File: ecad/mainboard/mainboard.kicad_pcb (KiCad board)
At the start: 12 copper layers, 26 parts, among them M1 Left Motor, M2 Right Motor, Q1 SS8050, Q2 SS8050, U1 LM358

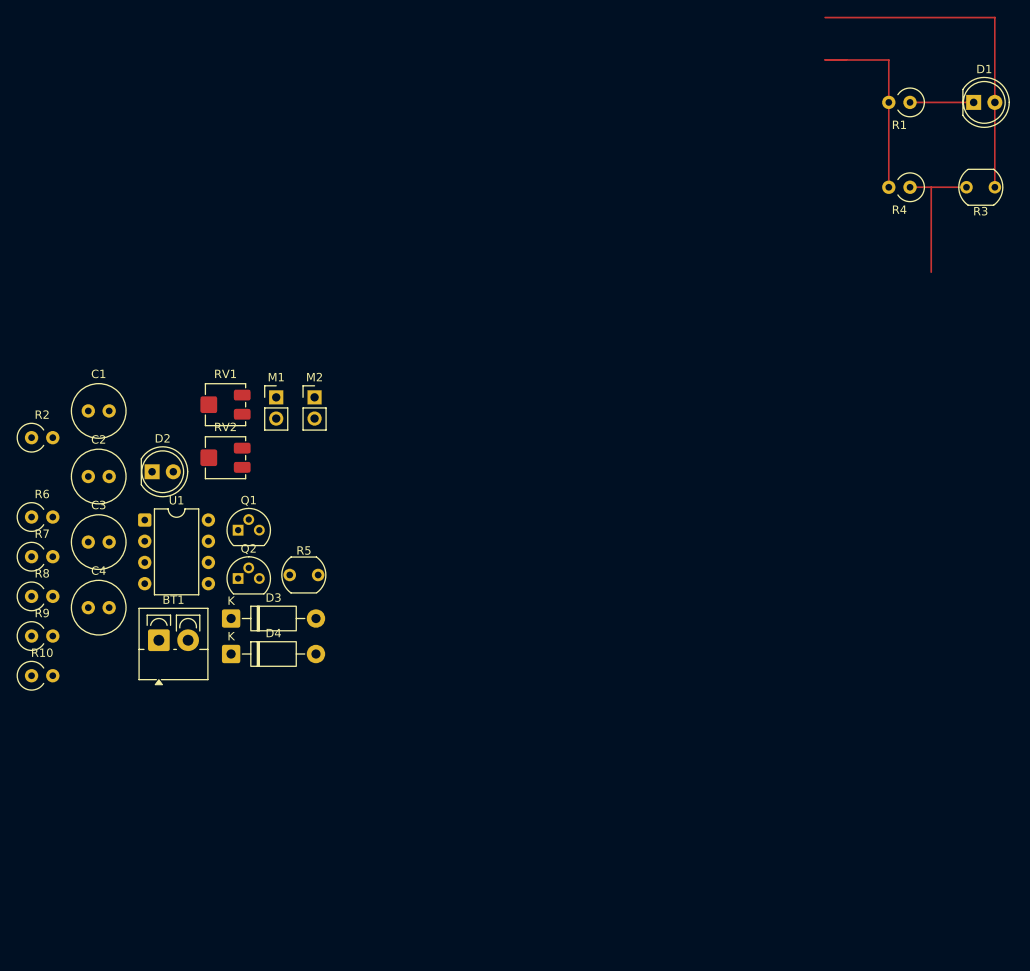
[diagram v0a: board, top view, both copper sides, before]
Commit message: update schematics with smd components
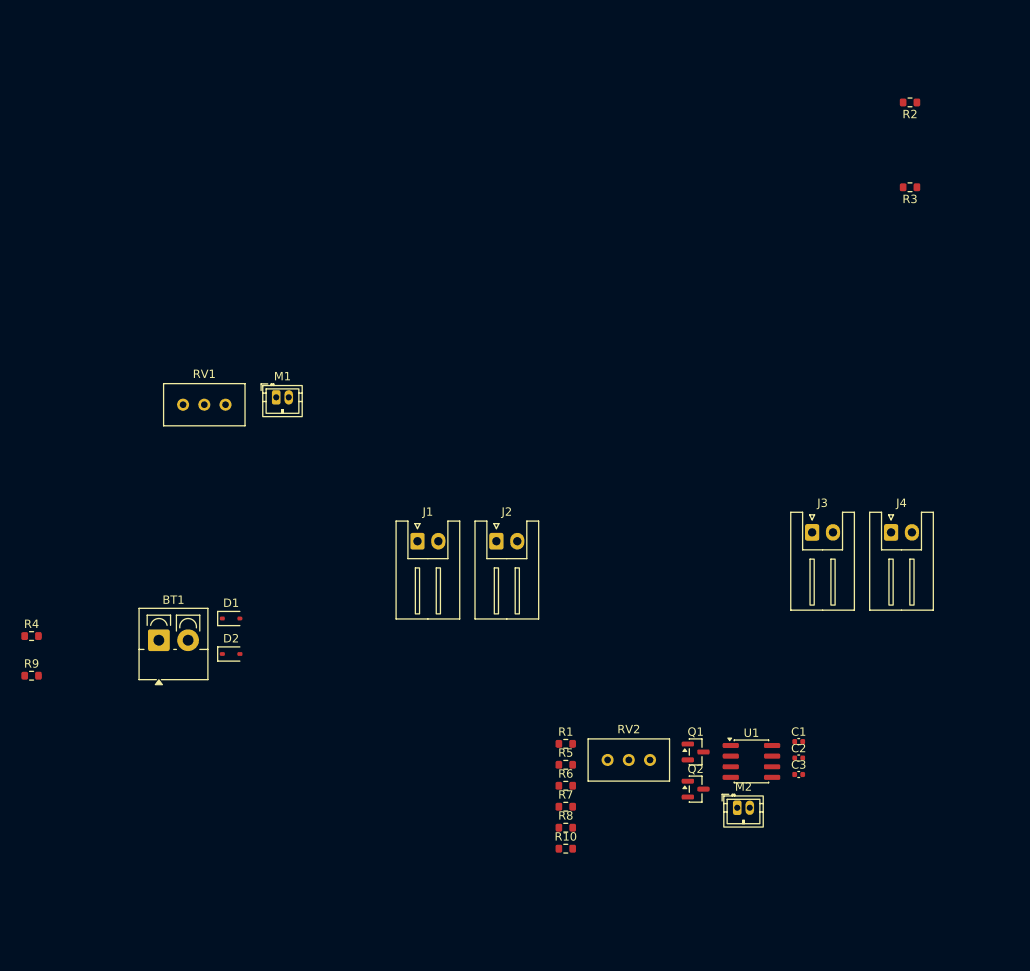
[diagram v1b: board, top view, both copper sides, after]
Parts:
- removed C4: 100uF, Capacitor_THT:C_Radial_D6.3mm_H11.0mm_P2.50mm
- removed the D1 at (180.3, 33.0)
- removed the D2 at (82.0, 77.2)
- removed the R2 at (67.5, 73.2)
- removed the R3 at (182.9, 43.2)
- added J1: IR LED, Connector_JST:JST_XH_S2B-XH-A_1x02_P2.50mm_Horizontal, F.Cu at (113.8, 85.6)
- added J2: IR Diode, Connector_JST:JST_XH_S2B-XH-A_1x02_P2.50mm_Horizontal, F.Cu at (123.2, 85.6)
- added J3: IR LED, Connector_JST:JST_XH_S2B-XH-A_1x02_P2.50mm_Horizontal, F.Cu at (161.0, 84.5)
- added J4: IR Diode, Connector_JST:JST_XH_S2B-XH-A_1x02_P2.50mm_Horizontal, F.Cu at (170.4, 84.5)
- added R1: 2.2k, Resistor_SMD:R_0603_1608Metric, F.Cu at (131.5, 109.8)
- added R10: 10k, Resistor_SMD:R_0603_1608Metric, F.Cu at (131.5, 122.4)
- C1, C2, C3: footprint Capacitor_THT:C_Radial_D6.3mm_H5.0mm_P2.50mm -> Capacitor_SMD:C_0402_1005Metric
- D1: renamed from D3; value 1N4007 -> 1N4148WS; footprint Diode_THT:D_DO-41_SOD81_P10.16mm_Horizontal -> Diode_SMD:D_SOD-323
- D2: renamed from D4; value 1N4007 -> 1N4148WS; footprint Diode_THT:D_DO-41_SOD81_P10.16mm_Horizontal -> Diode_SMD:D_SOD-323
- M1: value Left Motor -> Left N20 Motor; footprint Connector_PinHeader_2.54mm:PinHeader_1x02_P2.54mm_Vertical -> Connector_JST:JST_ZH_B2B-ZR_1x02_P1.50mm_Vertical
- M2: value Right Motor -> Right N20 Motor; footprint Connector_PinHeader_2.54mm:PinHeader_1x02_P2.54mm_Vertical -> Connector_JST:JST_ZH_B2B-ZR_1x02_P1.50mm_Vertical
- Q1, Q2: value SS8050 -> 2N7002; footprint Package_TO_SOT_THT:TO-92 -> Package_TO_SOT_SMD:SOT-23
- R2: renamed from R1; footprint Resistor_THT:R_Axial_DIN0309_L9.0mm_D3.2mm_P2.54mm_Vertical -> Resistor_SMD:R_0603_1608Metric
- R3: renamed from R4; footprint Resistor_THT:R_Axial_DIN0309_L9.0mm_D3.2mm_P2.54mm_Vertical -> Resistor_SMD:R_0603_1608Metric
- R4: renamed from R9; footprint Resistor_THT:R_Axial_DIN0309_L9.0mm_D3.2mm_P2.54mm_Vertical -> Resistor_SMD:R_0603_1608Metric
- R5: value LDR07 -> 10k; footprint OptoDevice:R_LDR_5.1x4.3mm_P3.4mm_Vertical -> Resistor_SMD:R_0603_1608Metric
- R6: value 10k -> 220; footprint Resistor_THT:R_Axial_DIN0309_L9.0mm_D3.2mm_P2.54mm_Vertical -> Resistor_SMD:R_0603_1608Metric
- R7: value 100k -> 10k; footprint Resistor_THT:R_Axial_DIN0309_L9.0mm_D3.2mm_P2.54mm_Vertical -> Resistor_SMD:R_0603_1608Metric
- R8: value 100k -> 2.2k; footprint Resistor_THT:R_Axial_DIN0309_L9.0mm_D3.2mm_P2.54mm_Vertical -> Resistor_SMD:R_0603_1608Metric
- R9: renamed from R10; footprint Resistor_THT:R_Axial_DIN0309_L9.0mm_D3.2mm_P2.54mm_Vertical -> Resistor_SMD:R_0603_1608Metric
- RV1, RV2: footprint Potentiometer_SMD:Potentiometer_Bourns_3214J_Horizontal -> Potentiometer_THT:Potentiometer_Bourns_3296W_Vertical
- U1: value LM358 -> LM393; footprint Package_DIP:DIP-8_W7.62mm -> Package_SO:SOIC-8_3.9x4.9mm_P1.27mm
- moved C1 93.8 mm to (159.4, 109.5)
- moved C2 91.5 mm to (159.4, 111.5)
- moved C3 89.5 mm to (159.4, 113.5)
- moved U1 78.2 mm to (153.7, 111.9)
- moved R6 71.6 mm to (131.5, 114.8)
- moved R7 70.6 mm to (131.5, 117.3)
- moved M2 70.5 mm to (152.0, 117.5)
- moved R8 69.7 mm to (131.5, 119.9)
- moved RV2 62.4 mm to (141.6, 111.7)
- moved Q1 60.9 mm to (147.1, 110.8)
- moved Q2 60.3 mm to (147.1, 115.2)
- moved R5 40.1 mm to (131.5, 112.3)
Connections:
- C2 pad 2: Net-(D4-A) -> GND
- C3 pad 2: GND -> Net-(D2-A)
- D2 pad 2: Net-(D4-A) -> Net-(D2-A)
- M2 pad 2: Net-(D4-A) -> Net-(D2-A)
- Q2 pad 3: Net-(D4-A) -> Net-(D2-A)
- R4 pad 1: Net-(R7-Pad2) -> Net-(R1-Pad1)
- R5 pad 1: +5V -> Net-(R1-Pad1)
- R5 pad 2: /sense2 -> GND
- R6 pad 1: /sense2 -> Net-(J3-Pin_2)
- R7 pad 1: /sense1 -> /sense2
- R7 pad 2: Net-(R7-Pad2) -> GND
- R8 pad 1: /sense2 -> Net-(R10-Pad1)
- R8 pad 2: Net-(R10-Pad1) -> +5V
- U1 pad 1: Net-(R7-Pad2) -> Net-(R1-Pad1)
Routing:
- net +5V: track 40.6 -> 0.00 mm
- net GND: track 25.4 -> 0.00 mm
- net /sense1: track 16.9 -> 0.00 mm
- net Net-(J1-Pin_2): track 7.62 -> 0.00 mm

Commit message: ecad: update footprints
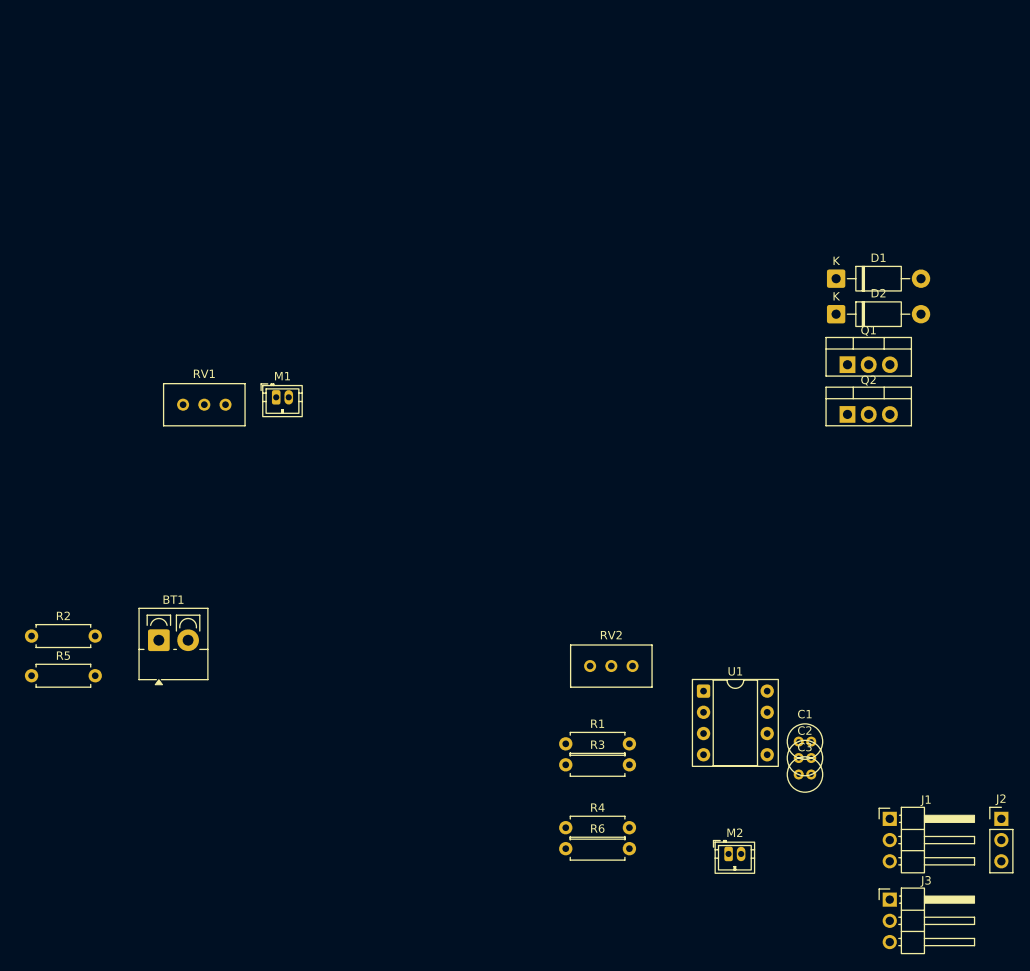
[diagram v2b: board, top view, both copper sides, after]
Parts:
- removed J4: IR Diode, Connector_JST:JST_XH_S2B-XH-A_1x02_P2.50mm_Horizontal
- removed the R2 at (172.7, 33.0)
- removed the R3 at (172.7, 43.2)
- removed the R6 at (131.5, 114.8)
- removed R7: 10k, Resistor_SMD:R_0603_1608Metric
- C1, C2, C3: footprint Capacitor_SMD:C_0402_1005Metric -> Capacitor_THT:C_Radial_D4.0mm_H7.0mm_P1.50mm
- D1, D2: value 1N4148WS -> 1N4001; footprint Diode_SMD:D_SOD-323 -> Diode_THT:D_DO-41_SOD81_P10.16mm_Horizontal
- J1, J3: value IR LED -> Conn_01x03_Pin; footprint Connector_JST:JST_XH_S2B-XH-A_1x02_P2.50mm_Horizontal -> Connector_PinHeader_2.54mm:PinHeader_1x03_P2.54mm_Horizontal
- J2: value IR Diode -> 3.3V Regulator; footprint Connector_JST:JST_XH_S2B-XH-A_1x02_P2.50mm_Horizontal -> Connector_PinHeader_2.54mm:PinHeader_1x03_P2.54mm_Vertical
- Q1, Q2: value 2N7002 -> IRLB8721PBF; footprint Package_TO_SOT_SMD:SOT-23 -> Package_TO_SOT_THT:TO-220-3_Vertical
- R1: footprint Resistor_SMD:R_0603_1608Metric -> Resistor_THT:R_Axial_DIN0207_L6.3mm_D2.5mm_P7.62mm_Horizontal
- R2: renamed from R4; footprint Resistor_SMD:R_0603_1608Metric -> Resistor_THT:R_Axial_DIN0207_L6.3mm_D2.5mm_P7.62mm_Horizontal
- R3: renamed from R5; footprint Resistor_SMD:R_0603_1608Metric -> Resistor_THT:R_Axial_DIN0207_L6.3mm_D2.5mm_P7.62mm_Horizontal
- R4: renamed from R8; footprint Resistor_SMD:R_0603_1608Metric -> Resistor_THT:R_Axial_DIN0207_L6.3mm_D2.5mm_P7.62mm_Horizontal
- R5: renamed from R9; footprint Resistor_SMD:R_0603_1608Metric -> Resistor_THT:R_Axial_DIN0207_L6.3mm_D2.5mm_P7.62mm_Horizontal
- R6: renamed from R10; footprint Resistor_SMD:R_0603_1608Metric -> Resistor_THT:R_Axial_DIN0207_L6.3mm_D2.5mm_P7.62mm_Horizontal
- U1: footprint Package_SO:SOIC-8_3.9x4.9mm_P1.27mm -> Package_DIP:DIP-8_W7.62mm_Socket
- moved D1 83.1 mm to (163.9, 54.1)
- moved D2 83.1 mm to (163.9, 58.4)
- moved J2 69.0 mm to (183.7, 118.8)
- moved J1 65.6 mm to (170.3, 118.8)
- moved Q1 49.8 mm to (165.2, 64.4)
- moved Q2 48.4 mm to (165.2, 70.4)
- moved J3 44.9 mm to (170.3, 128.5)
- moved RV2 11.4 mm to (139.5, 100.5)
- moved U1 10.2 mm to (148.0, 103.5)
- moved M2 5.63 mm to (151.0, 123.0)
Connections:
- BT1 pad 1: +5V -> +BATT
- C1 pad 1: +5V -> +3.3V
- C2 pad 1: +5V -> +3.3V
- C3 pad 1: +5V -> +3.3V
- D1 pad 1: +5V -> +3.3V
- D2 pad 1: +5V -> +3.3V
- J1 pad 1: +5V -> +3.3V
- J1 pad 2: Net-(J1-Pin_2) -> /sense1
- J2 pad 1: +5V -> +3.3V
- J2 pad 2: /sense1 -> GND
- J3 pad 1: +5V -> +3.3V
- J3 pad 2: Net-(J3-Pin_2) -> /sense2
- M1 pad 1: +5V -> +3.3V
- M2 pad 1: +5V -> +3.3V
- Q1 pad 2: GND -> Net-(D1-A)
- Q1 pad 3: Net-(D1-A) -> GND
- Q2 pad 2: GND -> Net-(D2-A)
- Q2 pad 3: Net-(D2-A) -> GND
- R1 pad 2: +5V -> +3.3V
- R4 pad 2: +5V -> +3.3V
- RV1 pad 1: +5V -> +3.3V
- RV2 pad 1: +5V -> +3.3V
- U1 pad 8: +5V -> +3.3V
